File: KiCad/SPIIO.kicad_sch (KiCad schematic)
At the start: 24 parts, among them J10 Conn_01x02, J11 Conn_01x02, J3 Conn_01x02, J4 Conn_01x02, J5 Conn_01x02, J6 Conn_01x02, J7 Conn_01x02, SW5 SW_SPDT, SW6 SW_SPDT, U10 74AHC595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

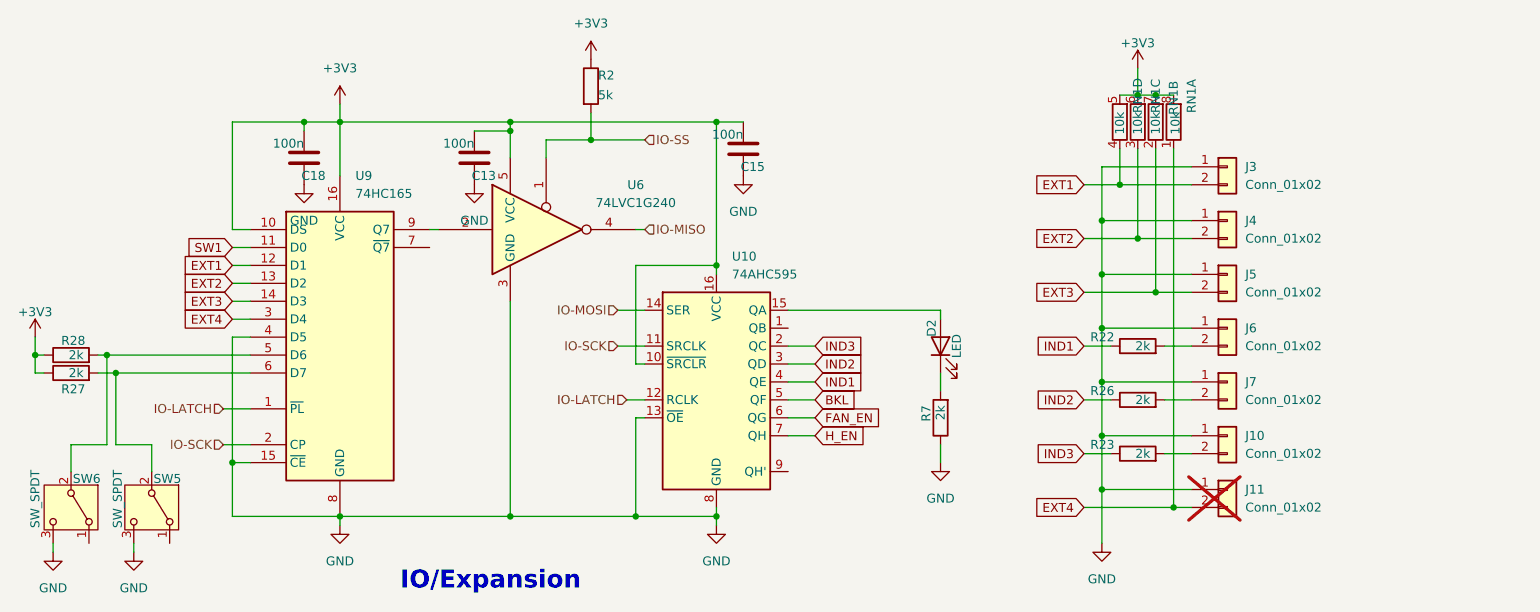
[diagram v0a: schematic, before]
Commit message: Update
Documentation related changes and small DRU corrections
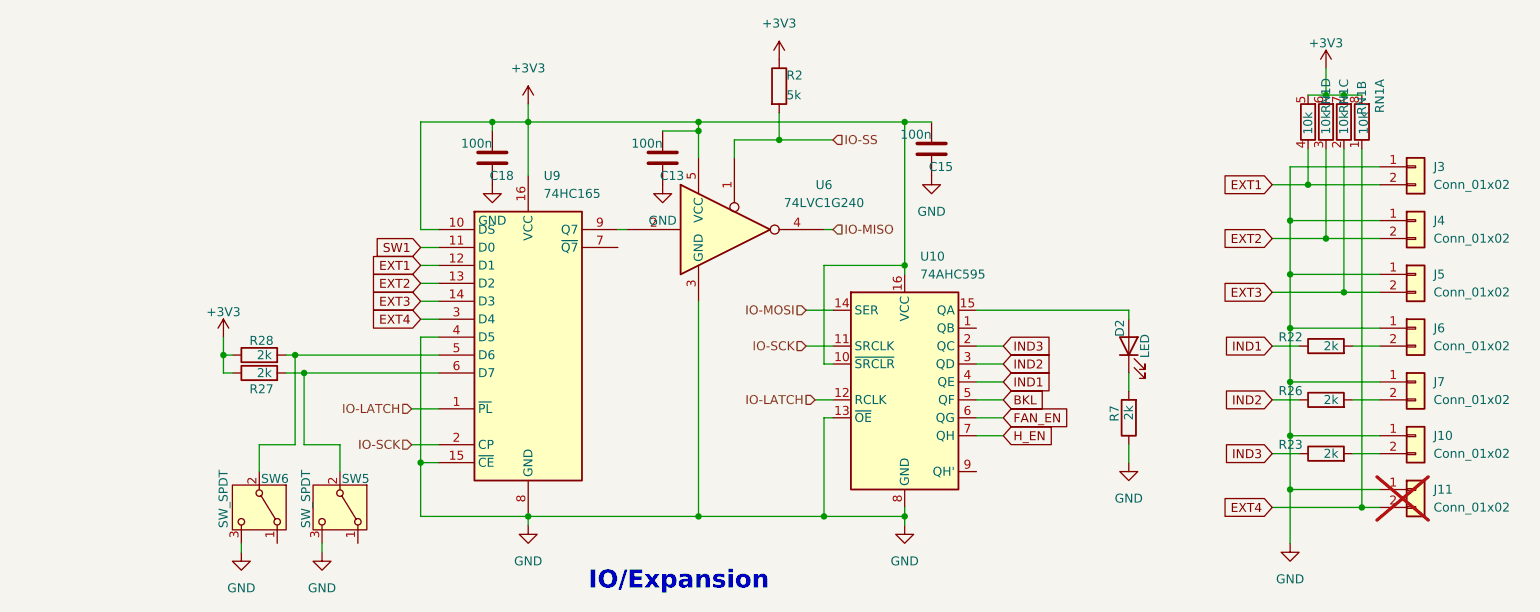
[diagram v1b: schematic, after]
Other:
- moved on the sheet: C13, C15, C18, D2, J10, J11, J3, J4, J5, J6, J7, R2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
